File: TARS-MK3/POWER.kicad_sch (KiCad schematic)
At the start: 48 parts, among them J1 Conn_02x12_Odd_Even, J2 Conn_02x12_Odd_Even, J3 Conn_02x12_Odd_Even, J4 Conn_02x12_Odd_Even, J5 AVRISP, U1 LK112M33TR, U2 ATmega328P-A, U3 D36V50F6, U4 D36V50F6, U5 D36V28F9, U6 D36V28F3, U7 D24V50F5, Y1 8Mhz

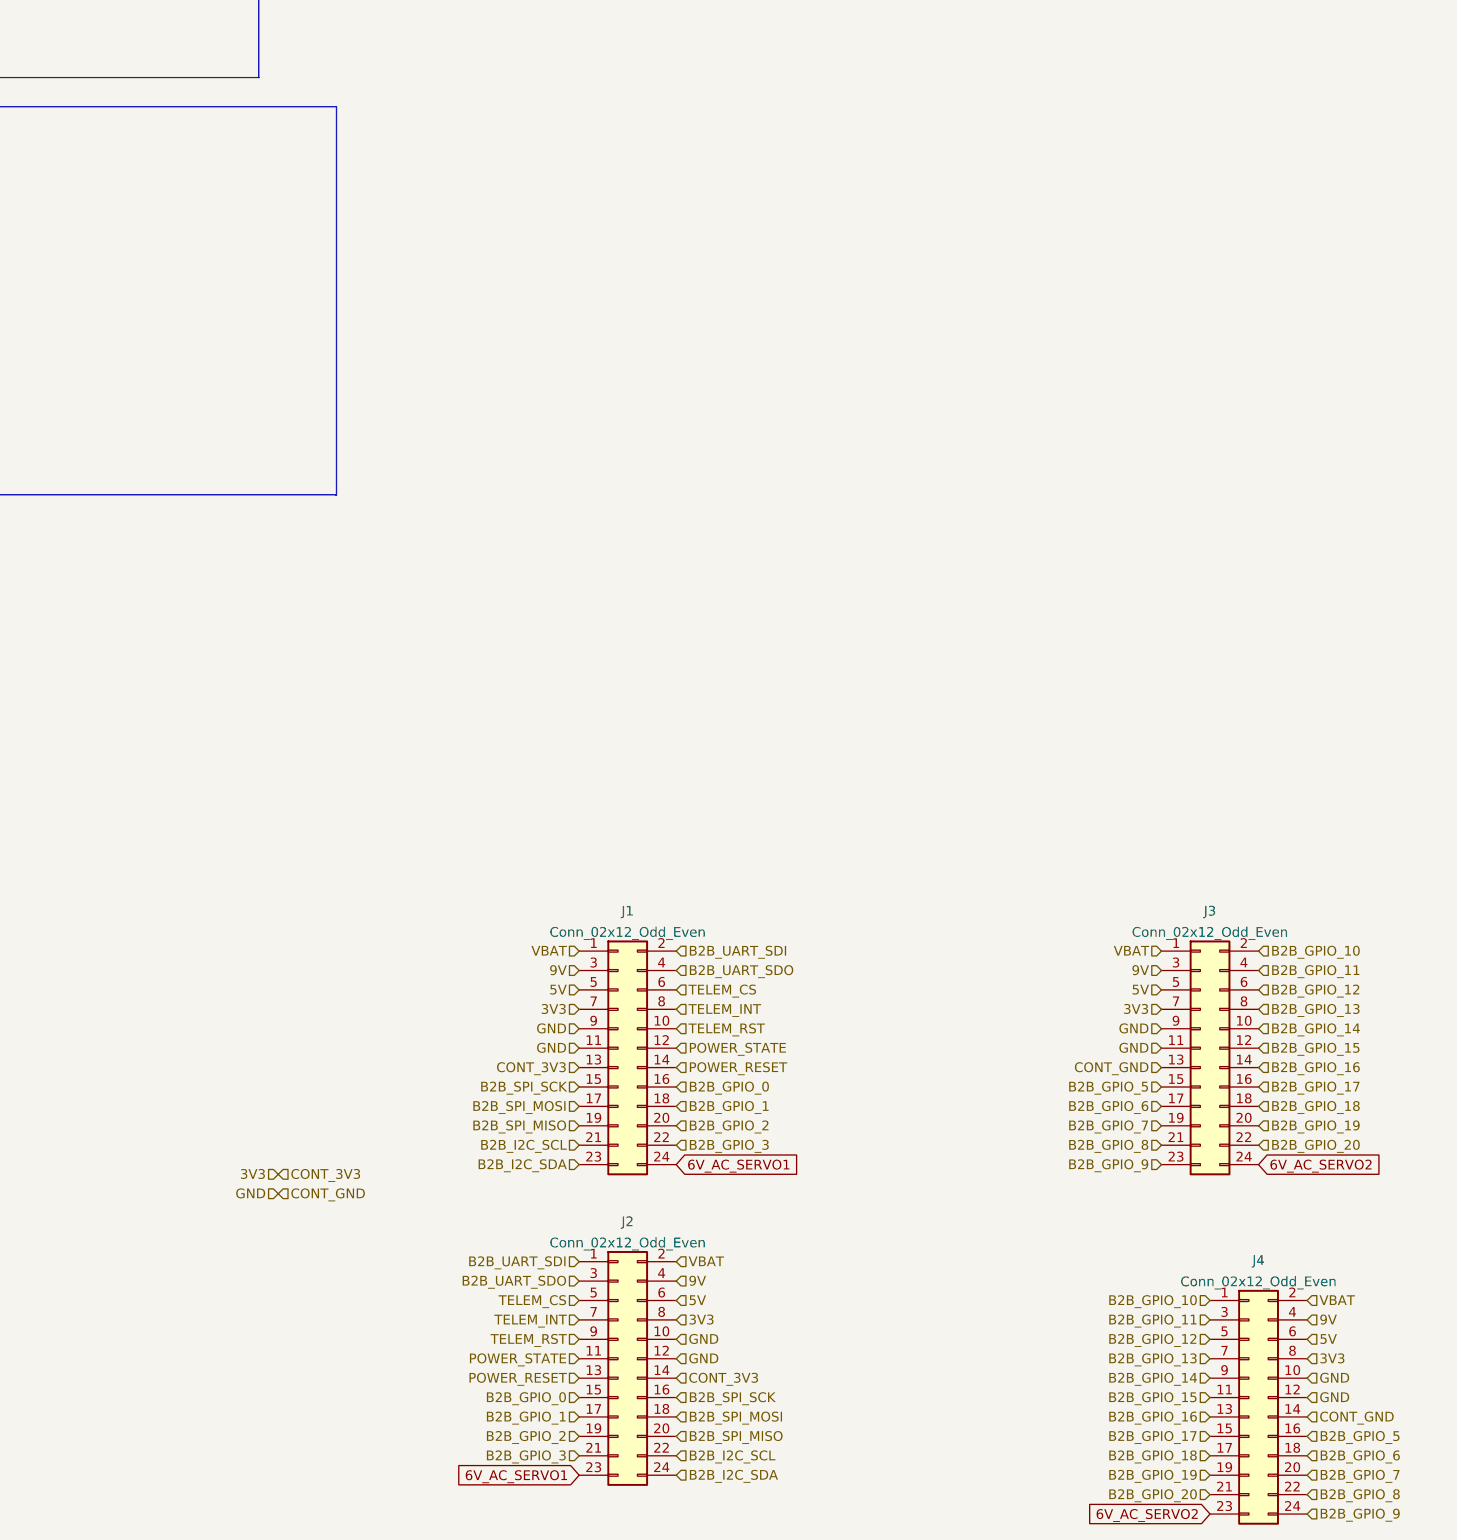
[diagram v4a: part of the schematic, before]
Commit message: allocated telemetry b2b and added battery connector
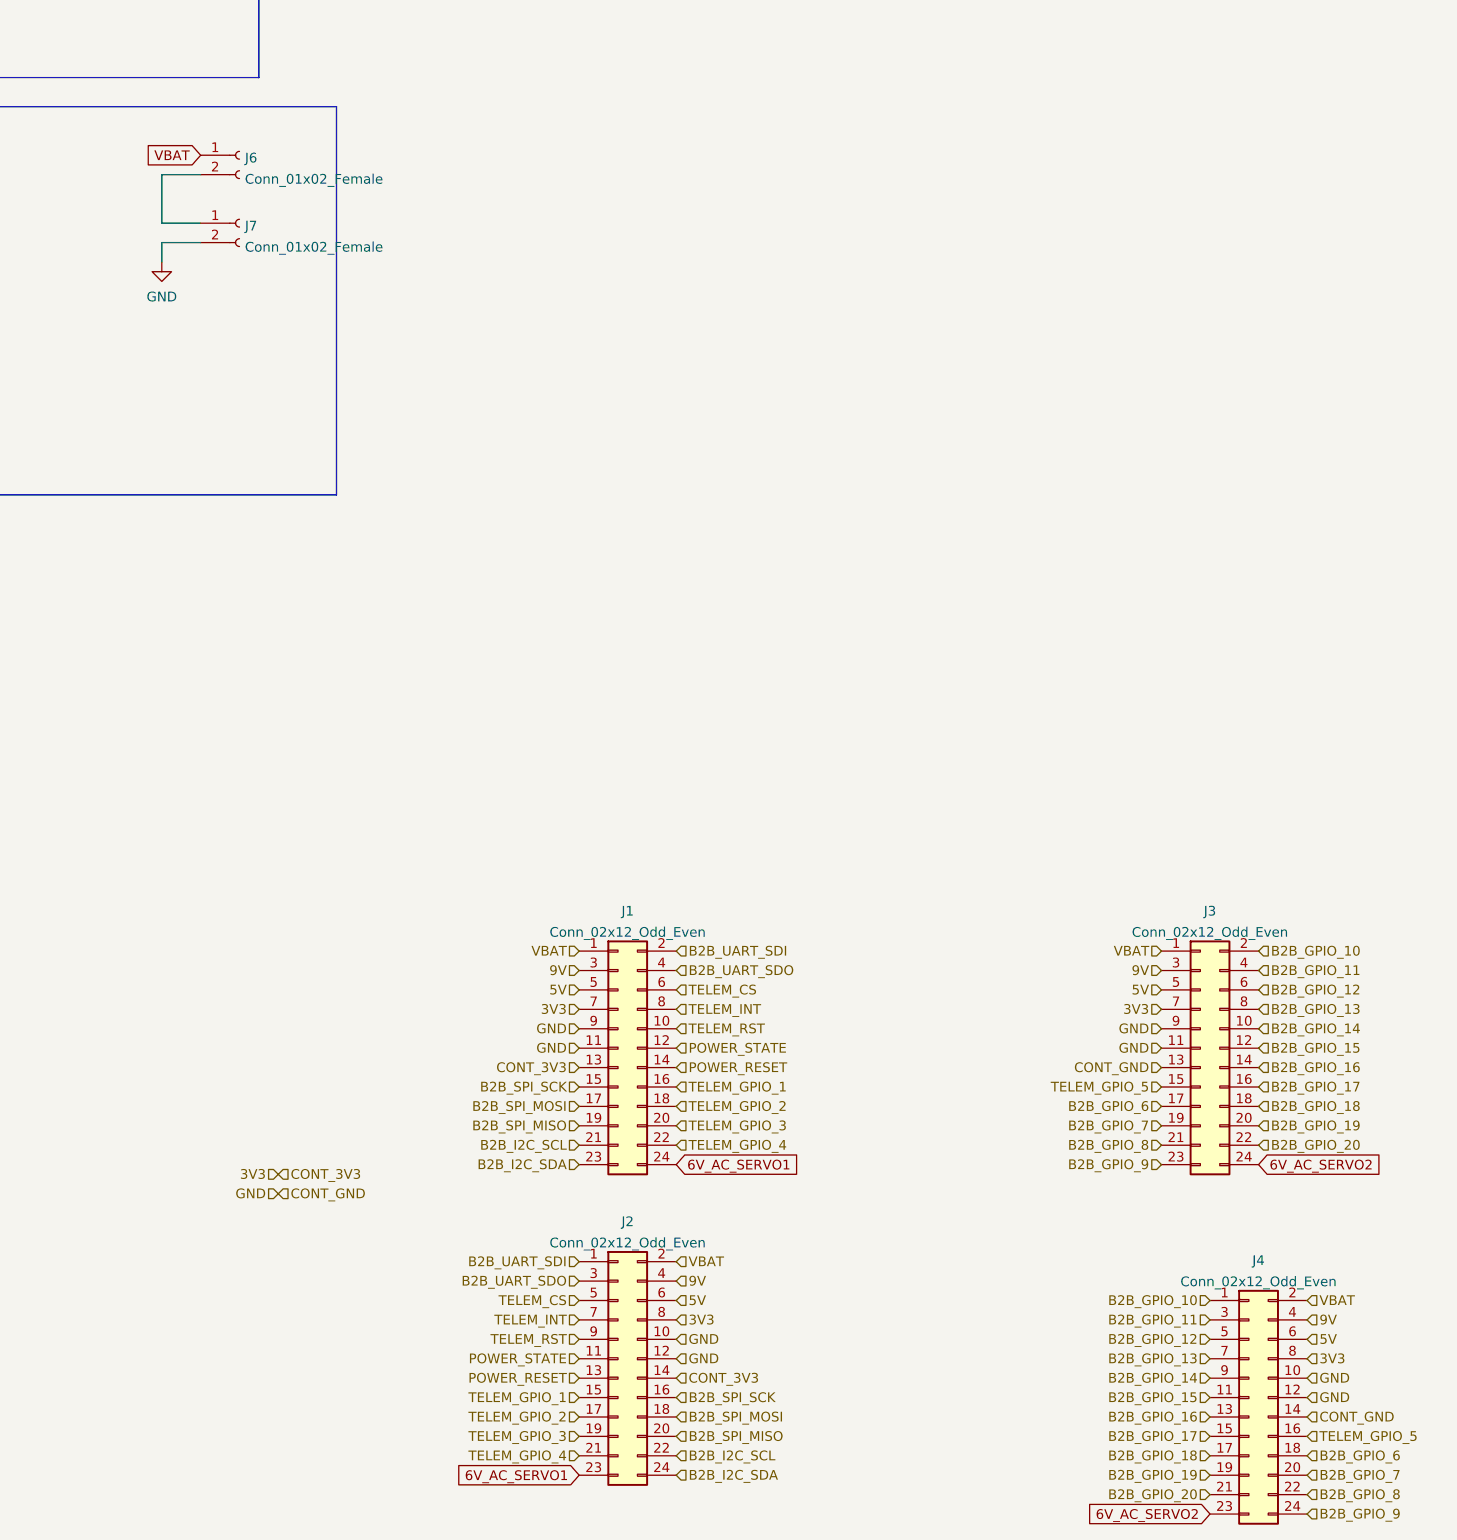
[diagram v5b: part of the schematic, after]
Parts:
- added J6: Conn_01x02_Female, Connector_AMASS:AMASS_XT60-F_1x02_P7.20mm_Vertical, symbol Connector:Conn_01x02_Female
- added J7: Conn_01x02_Female, Connector_Molex:Molex_CLIK-Mate_502443-0270_1x02-1MP_P2.00mm_Vertical, symbol Connector:Conn_01x02_Female
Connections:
- net GND: now also J7.2 (Pin_2)
- net VBAT: now also J6.1 (Pin_1)
- net B2B_GPIO_0 renamed TELEM_GPIO_1
- net B2B_GPIO_1 renamed TELEM_GPIO_2
- net B2B_GPIO_2 renamed TELEM_GPIO_3
- net B2B_GPIO_3 renamed TELEM_GPIO_4
- net B2B_GPIO_5 renamed TELEM_GPIO_5
- new net: J6.2 (Pin_2), J7.1 (Pin_1)

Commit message: PMB fixups
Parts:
- removed J6: Conn_01x02_Female, Connector_AMASS:AMASS_XT60-F_1x02_P7.20mm_Vertical, symbol Connector:Conn_01x02_Female
- added J6: Conn_01x03_Female, Connector_Molex:Molex_Micro-Fit_3.0_43650-0315_1x03_P3.00mm_Vertical, symbol Connector:Conn_01x03_Female
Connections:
- net GND: now also J6.2 (Pin_2)
- net VBAT: now also J6.1 (Pin_1)
- net at J7.1 (Pin_1): now also J6.3 (Pin_3)

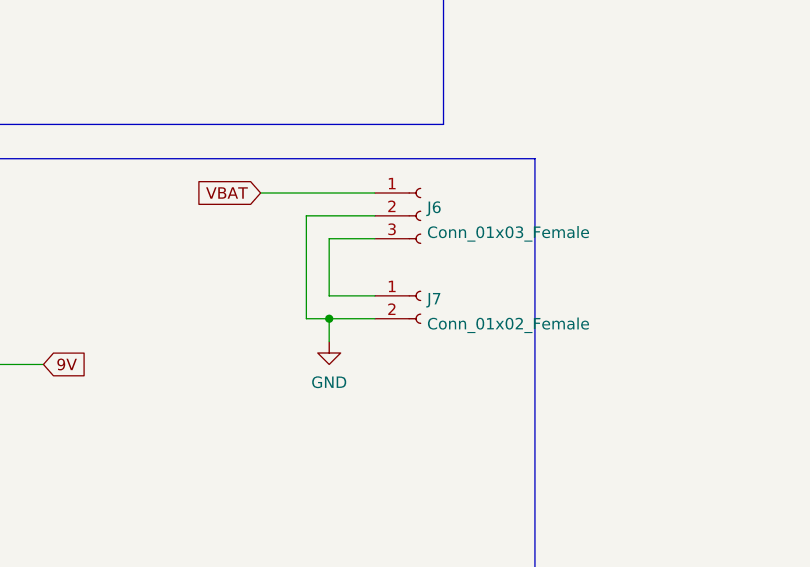
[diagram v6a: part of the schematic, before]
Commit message: moved connectors to top
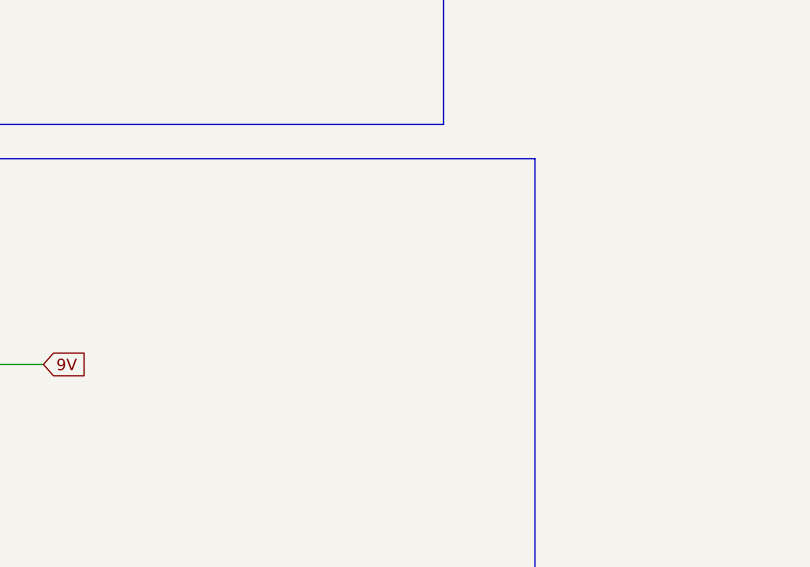
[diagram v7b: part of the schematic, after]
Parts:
- removed J6: Conn_01x03_Female, Connector_Molex:Molex_Micro-Fit_3.0_43650-0315_1x03_P3.00mm_Vertical, symbol Connector:Conn_01x03_Female
- removed J7: Conn_01x02_Female, Connector_Molex:Molex_CLIK-Mate_502443-0270_1x02-1MP_P2.00mm_Vertical, symbol Connector:Conn_01x02_Female
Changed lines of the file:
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@@
   (junction (at 212.09 48.26) (diameter 0) (color 0 0 0 0)
-  )
-  (junction (at 255.27 137.16) (diameter 0) (color 0 0 0 0)
   )
   (junction (at -22.86 69.85) (diameter 0) (color 0 0 0 0)
@@
     (stroke (width 0) (type default) (color 0 0 0 0))
   )
-  (wire (pts (xy 252.73 137.16) (xy 255.27 137.16))
-    (stroke (width 0) (type default) (color 0 0 0 0))
-  )
   (wire (pts (xy 153.67 -22.86) (xy 153.67 -13.97))
     (stroke (width 0) (type default) (color 0 0 0 0))
@@
     (stroke (width 0) (type default) (color 0 0 0 0))
   )
-  (wire (pts (xy 247.65 123.19) (xy 260.35 123.19))
-    (stroke (width 0) (type default) (color 0 0 0 0))
-  )
   (wire (pts (xy 57.15 134.62) (xy 59.69 134.62))
     (stroke (width 0) (type default) (color 0 0 0 0))
@@
     (stroke (width 0) (type default) (color 0 0 0 0))
   )
-  (wire (pts (xy 260.35 125.73) (xy 252.73 125.73))
-    (stroke (width 0) (type default) (color 0 0 0 0))
-  )
   (polyline (pts (xy 267.97 27.94) (xy 267.97 115.57))
     (stroke (width 0) (type default) (color 0 0 0 0))
@@
     (stroke (width 0) (type default) (color 0 0 0 0))
   )
-  (wire (pts (xy 255.27 128.27) (xy 255.27 134.62))
-    (stroke (width 0) (type default) (color 0 0 0 0))
-  )
   (wire (pts (xy 101.6 151.13) (xy 92.71 151.13))
     (stroke (width 0) (type default) (color 0 0 0 0))
@@
     (stroke (width 0) (type default) (color 0 0 0 0))
   )
-  (wire (pts (xy 255.27 137.16) (xy 255.27 139.7))
-    (stroke (width 0) (type default) (color 0 0 0 0))
-  )
   (wire (pts (xy 119.38 64.77) (xy 121.92 64.77))
     (stroke (width 0) (type default) (color 0 0 0 0))
@@
     (stroke (width 0) (type default) (color 0 0 0 0))
   )
-  (wire (pts (xy 255.27 134.62) (xy 260.35 134.62))
-    (stroke (width 0) (type default) (color 0 0 0 0))
-  )
   (wire (pts (xy 22.86 15.24) (xy 35.56 15.24))
     (stroke (width 0) (type default) (color 0 0 0 0))
@@
     (stroke (width 0) (type default) (color 0 0 0 0))
   )
-  (wire (pts (xy 260.35 137.16) (xy 255.27 137.16))
-    (stroke (width 0) (type default) (color 0 0 0 0))
-  )
   (wire (pts (xy -41.91 182.88) (xy -41.91 185.42))
     (stroke (width 0) (type default) (color 0 0 0 0))
@@
     (stroke (width 0) (type default) (color 0 0 0 0))
   )
-  (wire (pts (xy 252.73 125.73) (xy 252.73 137.16))
-    (stroke (width 0) (type default) (color 0 0 0 0))
-  )
   (wire (pts (xy 55.88 12.7) (xy 58.42 12.7))
     (stroke (width 0) (type default) (color 0 0 0 0))
@@
   )
   (wire (pts (xy 92.71 171.45) (xy 90.17 171.45))
-    (stroke (width 0) (type default) (color 0 0 0 0))
-  )
-  (wire (pts (xy 255.27 128.27) (xy 260.35 128.27))
     (stroke (width 0) (type default) (color 0 0 0 0))
   )
@@
     (effects (font (size 1.27 1.27)) (justify right))
     (property "Intersheet References" "${INTERSHEET_REFS}" (id 0) (at -28.7523 58.3406 0)
-      (effects (font (size 1.27 1.27)) (justify right) hide)
-    )
-  )
-  (global_label "VBAT" (shape input) (at 247.65 123.19 180) (fields_autoplaced)
-    (effects (font (size 1.27 1.27)) (justify right))
-    (property "Intersheet References" "${INTERSHEET_REFS}" (id 0) (at 240.8221 123.1106 0)
       (effects (font (size 1.27 1.27)) (justify right) hide)
     )
@@
     (pin "2")
   )
-  (symbol (lib_id "Connector:Conn_01x03_Female") (at 265.43 125.73 0) (unit 1)
-    (in_bom yes) (on_board yes) (fields_autoplaced)
-    (property "Reference" "J6" (id 0) (at 266.1412 124.8215 0)
-      (effects (font (size 1.27 1.27)) (justify left))
-    )
-    (property "Value" "Conn_01x03_Female" (id 1) (at 266.1412 127.5966 0)
-      (effects (font (size 1.27 1.27)) (justify left))
-    )
-    (property "Footprint" "Connector_Molex:Molex_Micro-Fit_3.0_43650-0315_1x03_P3.00mm_Vertical" (id 2) (at 265.43 125.73 0)
-      (effects (font (size 1.27 1.27)) hide)
-    )
-    (property "Datasheet" "~" (id 3) (at 265.43 125.73 0)
-      (effects (font (size 1.27 1.27)) hide)
-    )
-    (pin "1")
-    (pin "2")
-    (pin "3")
-  )
   (symbol (lib_id "D24V50F5:R_US") (at 170.18 138.43 180) (unit 1)
     (in_bom yes) (on_board yes) (fields_autoplaced)
@@
     (pin "1")
     (pin "2")
-  )
-  (symbol (lib_id "power:GND") (at 255.27 139.7 0) (mirror y) (unit 1)
-    (in_bom yes) (on_board yes) (fields_autoplaced)
-    (property "Reference" "#PWR0101" (id 0) (at 255.27 146.05 0)
-      (effects (font (size 1.27 1.27)) hide)
-    )
-    (property "Value" "GND" (id 1) (at 255.27 144.2625 0))
-    (property "Footprint" "" (id 2) (at 255.27 139.7 0)
-      (effects (font (size 1.27 1.27)) hide)
-    )
-    (property "Datasheet" "" (id 3) (at 255.27 139.7 0)
-      (effects (font (size 1.27 1.27)) hide)
-    )
-    (pin "1")
   )
   (symbol (lib_id "power:GND") (at 227.33 88.9 0) (unit 1)
@@
     (pin "9")
   )
-  (symbol (lib_id "Connector:Conn_01x02_Female") (at 265.43 134.62 0) (unit 1)
-    (in_bom yes) (on_board yes) (fields_autoplaced)
-    (property "Reference" "J7" (id 0) (at 266.1412 134.9815 0)
-      (effects (font (size 1.27 1.27)) (justify left))
-    )
-    (property "Value" "Conn_01x02_Female" (id 1) (at 266.1412 137.7566 0)
-      (effects (font (size 1.27 1.27)) (justify left))
-    )
-    (property "Footprint" "Connector_Molex:Molex_CLIK-Mate_502443-0270_1x02-1MP_P2.00mm_Vertical" (id 2) (at 265.43 134.62 0)
-      (effects (font (size 1.27 1.27)) hide)
-    )
-    (property "Datasheet" "~" (id 3) (at 265.43 134.62 0)
-      (effects (font (size 1.27 1.27)) hide)
-    )
-    (pin "1")
-    (pin "2")
-  )
   (symbol (lib_id "D24V50F5:Crystal") (at 124.46 60.96 90) (unit 1)
     (in_bom yes) (on_board yes)
@@
       (reference "#PWR021") (unit 1) (value "GND") (footprint "")
     )
-    (path "/82037bc0-ca1b-427c-a91b-c1d959a7ead4"
-      (reference "#PWR0101") (unit 1) (value "GND") (footprint "")
-    )
     (path "/d4d4fa68-34f2-4653-bbf0-2d24f29cf971"
       (reference "C1") (unit 1) (value "LOAD_C") (footprint "Capacitor_SMD:C_0805_2012Metric")
@@
       (reference "J5") (unit 1) (value "AVRISP") (footprint "Connector_PinSocket_2.54mm:PinSocket_2x03_P2.54mm_Vertical")
     )
-    (path "/66c89329-6661-46fd-b4c5-7db91af0050f"
-      (reference "J6") (unit 1) (value "Conn_01x03_Female") (footprint "Connector_Molex:Molex_Micro-Fit_3.0_43650-0315_1x03_P3.00mm_Vertical")
-    )
-    (path "/d852d4ee-0fbe-40e5-9cd2-facf49e94f0e"
-      (reference "J7") (unit 1) (value "Conn_01x02_Female") (footprint "Connector_Molex:Molex_CLIK-Mate_502443-0270_1x02-1MP_P2.00mm_Vertical")
-    )
     (path "/ebdaa12a-f436-45e2-86d2-ef38b1ccd3b8"

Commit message: stuff
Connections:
- net B2B_SPI_MISO is gone; now on net AVR_MISO: J1.19 (Pin_19), J2.20 (Pin_20)
- net B2B_SPI_MOSI is gone; now on net AVR_MOSI: J1.17 (Pin_17), J2.18 (Pin_18)
- net B2B_SPI_SCK is gone; now on net AVR_SCK: J1.15 (Pin_15), J2.16 (Pin_16)
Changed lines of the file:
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@@
     (effects (font (size 1.27 1.27)) (justify left))
   )
-  (hierarchical_label "SNS_SPI_MISO" (shape input) (at 143.51 38.1 0)
+  (hierarchical_label "B2B_SPI_MISO" (shape input) (at 143.51 38.1 0)
     (effects (font (size 1.27 1.27)) (justify left))
   )
@@
     (effects (font (size 1.27 1.27)) (justify left))
   )
-  (hierarchical_label "SNS_SPI_MOSI" (shape input) (at 143.51 40.64 0)
+  (hierarchical_label "B2B_SPI_MOSI" (shape input) (at 143.51 40.64 0)
     (effects (font (size 1.27 1.27)) (justify left))
   )
@@
     (effects (font (size 1.27 1.27)) (justify left))
   )
-  (hierarchical_label "SNS_SPI_SCK" (shape input) (at 143.51 35.56 0)
+  (hierarchical_label "B2B_SPI_SCK" (shape input) (at 143.51 35.56 0)
     (effects (font (size 1.27 1.27)) (justify left))
   )
